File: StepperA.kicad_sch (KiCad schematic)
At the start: 19 parts

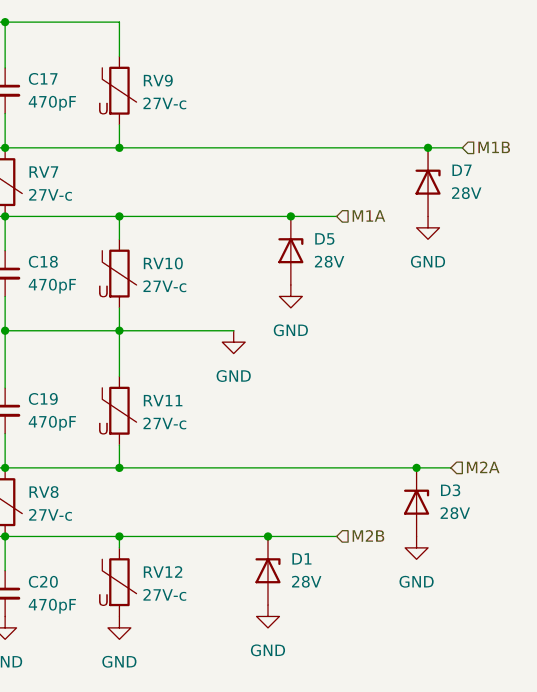
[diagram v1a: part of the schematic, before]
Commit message: added zener diodes
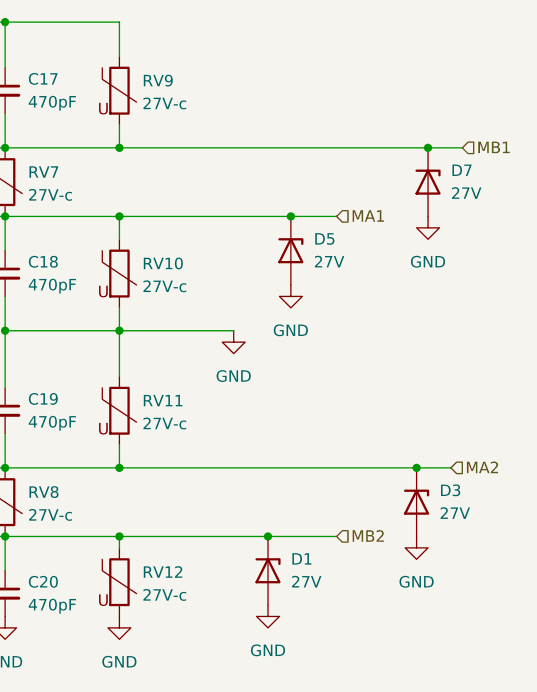
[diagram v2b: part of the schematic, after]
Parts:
- C17, C18, C19, C20: footprint (none) -> Capacitor_SMD:C_0603_1608Metric
- D1, D3, D5, D7: value 28V -> 27V
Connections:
- net M1A renamed MA1
- net M1B renamed MB1
- net M2A renamed MA2
- net M2B renamed MB2
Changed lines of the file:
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@@
 		)
 	)
-	(hierarchical_label "M2A"
+	(hierarchical_label "MA2"
 		(shape input)
 		(at 172.72 90.17 0)
@@
 		)
 	)
-	(hierarchical_label "M1A"
+	(hierarchical_label "MA1"
 		(shape input)
 		(at 160.02 62.23 0)
@@
 		)
 	)
-	(hierarchical_label "M1B"
+	(hierarchical_label "MB1"
 		(shape input)
 		(at 173.99 54.61 0)
@@
 		)
 	)
-	(hierarchical_label "M2B"
+	(hierarchical_label "MB2"
 		(shape input)
 		(at 160.02 97.79 0)
@@
 			)
 		)
-		(property "Footprint" ""
+		(property "Footprint" "Capacitor_SMD:C_0603_1608Metric"
 			(at 123.19 83.82 0)
 			(effects
@@
 			)
 		)
-		(property "Footprint" ""
+		(property "Footprint" "Capacitor_SMD:C_0603_1608Metric"
 			(at 123.19 48.26 0)
 			(effects
@@
 			)
 		)
-		(property "Value" "28V"
+		(property "Value" "27V"
 			(at 172.72 59.6899 90)
 			(effects
@@
 			)
 		)
-		(property "Value" "28V"
+		(property "Value" "27V"
 			(at 154.94 102.8699 90)
 			(effects
@@
 			)
 		)
-		(property "Value" "28V"
+		(property "Value" "27V"
 			(at 171.45 95.2499 90)
 			(effects
@@
 			)
 		)
-		(property "Footprint" ""
+		(property "Footprint" "Capacitor_SMD:C_0603_1608Metric"
 			(at 123.19 104.14 0)
 			(effects
@@
 			)
 		)
-		(property "Value" "28V"
+		(property "Value" "27V"
 			(at 157.48 67.3099 90)
 			(effects
@@
 			)
 		)
-		(property "Footprint" ""
+		(property "Footprint" "Capacitor_SMD:C_0603_1608Metric"
 			(at 123.19 68.58 0)
 			(effects

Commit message: UPDATE
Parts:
- D1, D3, D5, D7: footprint (none) -> Diode_SMD:D_0603_1608Metric
- L6, L7, L8, L9: footprint (none) -> iclr:IND_FDSD0630-H-1R0M=P3
- RV10, RV11, RV12, RV7, RV8, RV9: footprint (none) -> iclr:SDR1307A101K
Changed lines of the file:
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@@
 			)
 		)
-		(property "Footprint" ""
+		(property "Footprint" "Diode_SMD:D_0603_1608Metric"
 			(at 170.18 58.42 0)
 			(effects
@@
 			)
 		)
-		(property "Footprint" ""
+		(property "Footprint" "Diode_SMD:D_0603_1608Metric"
 			(at 152.4 101.6 0)
 			(effects
@@
 			)
 		)
-		(property "Footprint" ""
+		(property "Footprint" "Diode_SMD:D_0603_1608Metric"
 			(at 168.91 93.98 0)
 			(effects
@@
 			)
 		)
-		(property "Footprint" ""
+		(property "Footprint" "iclr:SDR1307A101K"
 			(at 134.112 102.87 90)
 			(effects
@@
 			)
 		)
-		(property "Footprint" ""
+		(property "Footprint" "Diode_SMD:D_0603_1608Metric"
 			(at 154.94 66.04 0)
 			(effects
@@
 			)
 		)
-		(property "Footprint" ""
+		(property "Footprint" "iclr:SDR1307A101K"
 			(at 134.112 83.82 90)
 			(effects
@@
 			)
 		)
-		(property "Footprint" ""
+		(property "Footprint" "iclr:IND_FDSD0630-H-1R0M=P3"
 			(at 115.57 90.17 0)
 			(effects
@@
 			)
 		)
-		(property "Footprint" ""
+		(property "Footprint" "iclr:SDR1307A101K"
 			(at 134.112 48.26 90)
 			(effects
@@
 			)
 		)
-		(property "Footprint" ""
+		(property "Footprint" "iclr:IND_FDSD0630-H-1R0M=P3"
 			(at 115.57 54.61 0)
 			(effects
@@
 			)
 		)
-		(property "Footprint" ""
+		(property "Footprint" "iclr:IND_FDSD0630-H-1R0M=P3"
 			(at 115.57 97.79 0)
 			(effects
@@
 			)
 		)
-		(property "Footprint" ""
+		(property "Footprint" "iclr:SDR1307A101K"
 			(at 134.112 68.58 90)
 			(effects
@@
 			)
 		)
-		(property "Footprint" ""
+		(property "Footprint" "iclr:IND_FDSD0630-H-1R0M=P3"
 			(at 115.57 62.23 0)
 			(effects
@@
 			)
 		)
-		(property "Footprint" ""
+		(property "Footprint" "iclr:SDR1307A101K"
 			(at 121.412 58.42 90)
 			(effects
@@
 			)
 		)
-		(property "Footprint" ""
+		(property "Footprint" "iclr:SDR1307A101K"
 			(at 121.412 93.98 90)
 			(effects

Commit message: update 2 everything is fixed
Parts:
- RV10, RV11, RV12, RV7, RV8, RV9: footprint iclr:SDR1307A101K -> Resistor_SMD:R_0805_2012Metric
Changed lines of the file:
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@@
 			)
 		)
-		(property "Footprint" "iclr:SDR1307A101K"
+		(property "Footprint" "Resistor_SMD:R_0805_2012Metric"
 			(at 134.112 102.87 90)
 			(effects
@@
 			)
 		)
-		(property "Footprint" "iclr:SDR1307A101K"
+		(property "Footprint" "Resistor_SMD:R_0805_2012Metric"
 			(at 134.112 83.82 90)
 			(effects
@@
 			)
 		)
-		(property "Footprint" "iclr:SDR1307A101K"
+		(property "Footprint" "Resistor_SMD:R_0805_2012Metric"
 			(at 134.112 48.26 90)
 			(effects
@@
 			)
 		)
-		(property "Footprint" "iclr:SDR1307A101K"
+		(property "Footprint" "Resistor_SMD:R_0805_2012Metric"
 			(at 134.112 68.58 90)
 			(effects
@@
 			)
 		)
-		(property "Footprint" "iclr:SDR1307A101K"
+		(property "Footprint" "Resistor_SMD:R_0805_2012Metric"
 			(at 121.412 58.42 90)
 			(effects
@@
 			)
 		)
-		(property "Footprint" "iclr:SDR1307A101K"
+		(property "Footprint" "Resistor_SMD:R_0805_2012Metric"
 			(at 121.412 93.98 90)
 			(effects

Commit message: finished pcb layouts, ready for check p sure
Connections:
- net MA2: now also C17.2, D7.1 (K), L6.2, RV7.1, RV9.2; no longer C19.2, D3.1 (K), L8.2, RV11.2, RV8.1
- net MB1: now also C19.2, D3.1 (K), L8.2, RV11.2, RV8.1; no longer C17.2, D7.1 (K), L6.2, RV7.1, RV9.2
- net 1B: now reaches L8.1
- net 1B: now also A1.4 (1B); no longer A1.6 (2A)
- net 2A: now reaches L6.1
- net 2A: now also A1.6 (2A); no longer A1.4 (1B)
- net 2B: now reaches A1.3 (2B), L9.1
- net 1A: now reaches A1.5 (1A), L7.1
- net +BATTV renamed VMAIN

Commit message: update
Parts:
- removed D1, D3, D5, D7: 27V, Diode_SMD:D_0603_1608Metric, symbol Device:D_Zener
- added D1, D2, D3, D4: D_Zener_Dual_CommonAnode_KKA, Package_TO_SOT_SMD:TSOT-23, symbol Device:D_Zener_Dual_CommonAnode_KKA
- L6, L7, L8, L9: footprint iclr:IND_FDSD0630-H-1R0M=P3 -> Inductor_SMD:L_0603_1608Metric
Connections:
- net GND: now also D1.1 (K), D2.2 (K), D3.1 (K), D4.2 (K)
- net MA1: now also D2.1 (K)
- net MA2: now also D1.2 (K)
- net MB1: now also D3.2 (K)
- net MB2: now also D4.1 (K)
- no-connect marks 0 -> 4

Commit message: update
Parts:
- L6, L7, L8, L9: value 80nH -> 4.7uH; footprint Inductor_SMD:L_0603_1608Metric -> iclr:MPLAL60504R7
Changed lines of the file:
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@@
 			)
 		)
-		(property "Value" "80nH"
+		(property "Value" "4.7uH"
 			(at 115.57 87.63 90)
 			(effects
@@
 			)
 		)
-		(property "Footprint" "Inductor_SMD:L_0603_1608Metric"
+		(property "Footprint" "iclr:MPLAL60504R7"
 			(at 115.57 90.17 0)
 			(effects
@@
 			)
 		)
-		(property "Value" "80nH"
+		(property "Value" "4.7uH"
 			(at 115.57 52.07 90)
 			(effects
@@
 			)
 		)
-		(property "Footprint" "Inductor_SMD:L_0603_1608Metric"
+		(property "Footprint" "iclr:MPLAL60504R7"
 			(at 115.57 54.61 0)
 			(effects
@@
 			)
 		)
-		(property "Value" "80nH"
+		(property "Value" "4.7uH"
 			(at 115.57 95.25 90)
 			(effects
@@
 			)
 		)
-		(property "Footprint" "Inductor_SMD:L_0603_1608Metric"
+		(property "Footprint" "iclr:MPLAL60504R7"
 			(at 115.57 97.79 0)
 			(effects
@@
 			)
 		)
-		(property "Value" "80nH"
+		(property "Value" "4.7uH"
 			(at 115.57 59.69 90)
 			(effects
@@
 			)
 		)
-		(property "Footprint" "Inductor_SMD:L_0603_1608Metric"
+		(property "Footprint" "iclr:MPLAL60504R7"
 			(at 115.57 62.23 0)
 			(effects
